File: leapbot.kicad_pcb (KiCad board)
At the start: 2 copper layers, 100 x 100 mm, 97 parts, among them J1 629105150521, J2 Conn_01x04_Male, J3 BM06B-SRSS-TB, J4 BM06B-SRSS-TB, Q1 FDV301N, Q2 FDV301N, SW1 1825910-6, SW2 1825910-6, U1 QRE1113GR, U10 DRV8872DDA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

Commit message: Add silkscreen annotations and logo, update titleblocks
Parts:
- added SYM1: LOGO, leapbot:logo, F.Cu at (84.5, 132.2)
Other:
- board text added: "+"
- board text added: "-"
- board text added: "3S BATTERY"
- board text added: "BATT"
- board text added: "BOOT"
- board text added: "ESP32"
- board text added: "LED0"
- board text added: "LED1"
- board text added: "LED2"
- board text added: "LED3"
- board text added: "LED4"
- board text added: "LED5"
- board text added: "LED6"
- board text added: "LED7"
- board text added: "LeapBot Rev 0.0.0 - 2020 github.com/hoani"
- board text added: "MOTOR LEFT"
- board text added: "MOTOR RIGHT"
- board text added: "RESET"

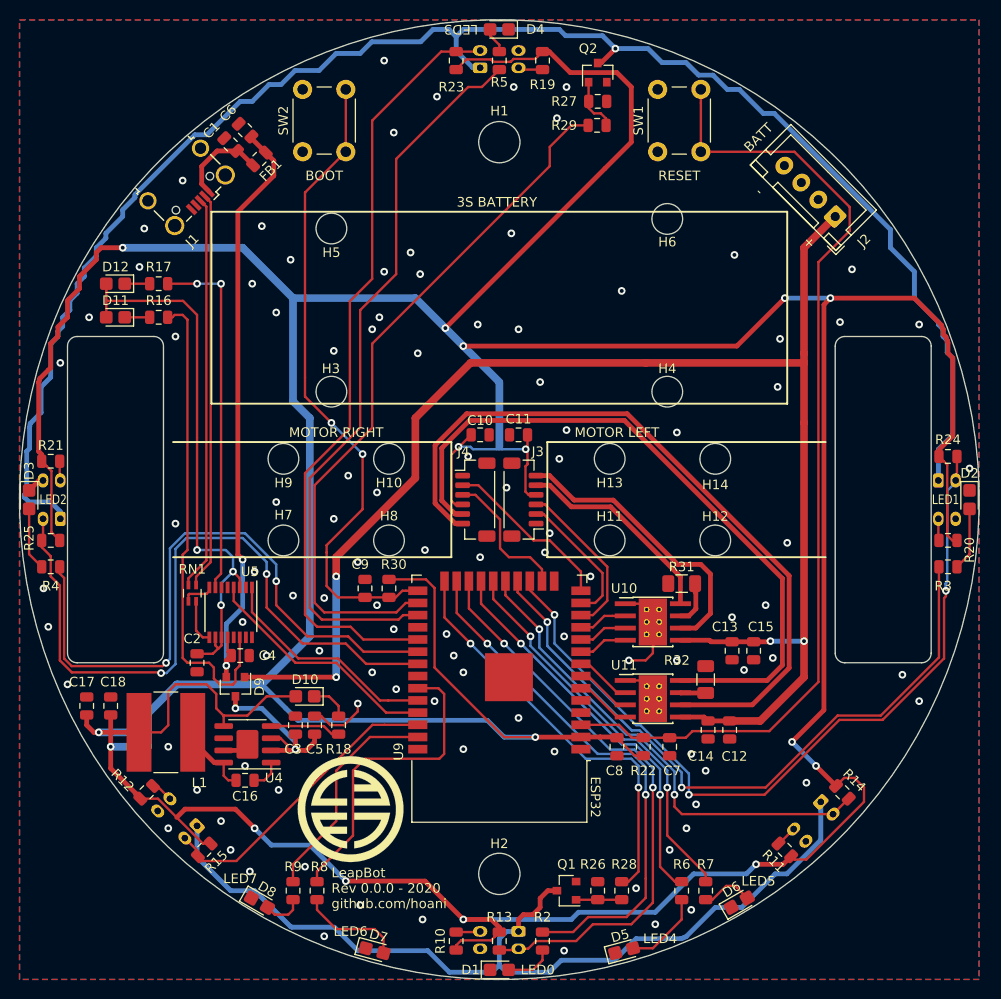
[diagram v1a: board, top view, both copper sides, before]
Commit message: Corrected some ADC assignments
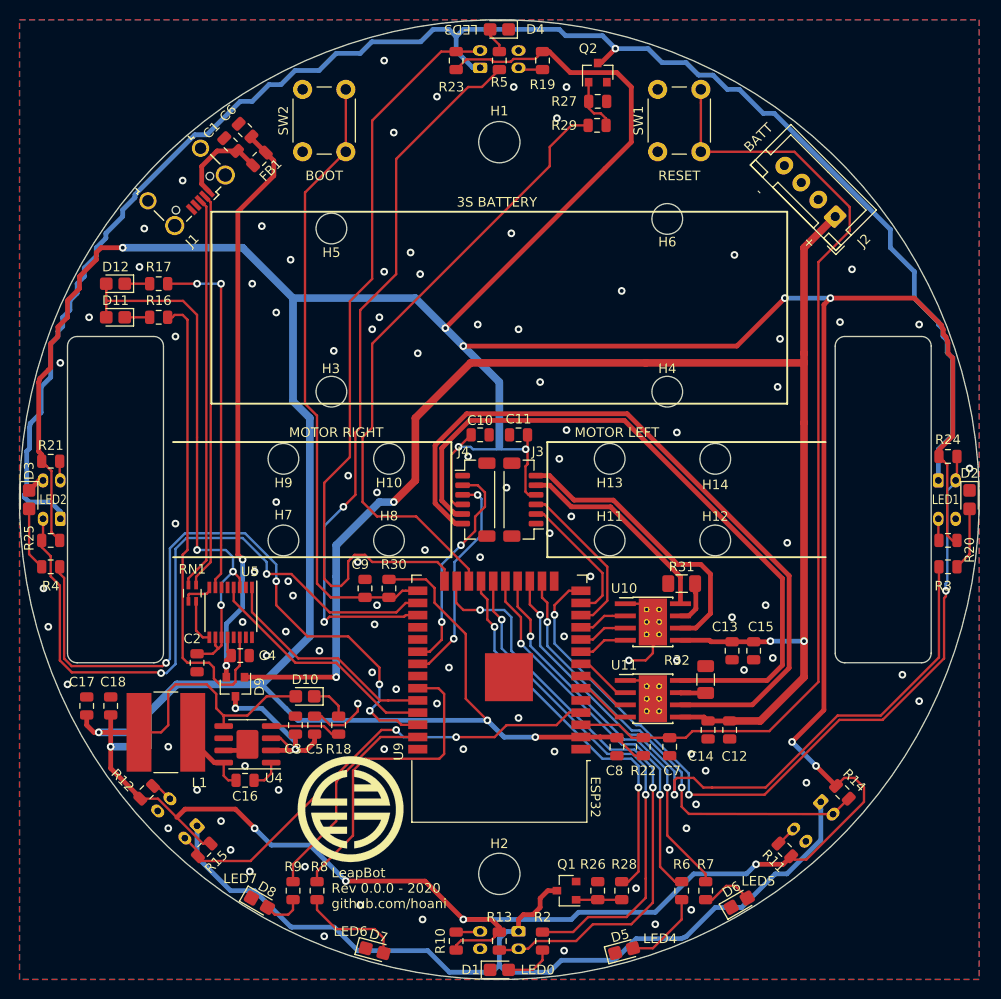
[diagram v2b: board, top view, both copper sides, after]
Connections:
- U9 pad 14: /M2_EB -> /LS_BL
- U9 pad 16: /M2_EA -> /LS_FL
- U9 pad 17: /LS_BL -> /LED1
- U9 pad 18: /LED1 -> /LED5
- U9 pad 19: /LS_FL -> /LED4
- U9 pad 20: /LED5 -> /LED0
- U9 pad 21: /LED4 -> /LS_PF
- U9 pad 22: /LS_FF -> /LS_PB
- U9 pad 23: /LED0 -> /LS_FF
- U9 pad 24: /LS_PF -> /LS_BB
- U9 pad 26: /LS_PB -> /LS_BR
- U9 pad 29: /LS_BB -> Net-(U9-Pad29)
- U9 pad 30: /LED2 -> /M2_EB
- U9 pad 31: /LS_BR -> /M2_EA
- U9 pad 36: /LS_FR -> /LED2
- U9 pad 4: Net-(U9-Pad4) -> /LS_FR
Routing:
- net /LS_FR: track 31.5 -> 49.6 mm, vias 0 -> 2
- net /LS_PB: track 74.2 -> 65.2 mm
- net /M2_EA: track 14.5 -> 22.7 mm, vias 0 -> 2
- net /LED2: track 67.0 -> 74.2 mm, vias 2 -> 4
- net +3V3: track 585.2 -> 579.5 mm, vias 16 -> 17
- net /M2_EB: track 18.0 -> 22.9 mm, vias 0 -> 2
- net /LS_BR: track 74.5 -> 70.6 mm
- net /LS_FF: track 61.0 -> 64.0 mm
- net /LED1: track 70.9 -> 73.7 mm
- net /BOOT_OP: track 67.8 -> 65.2 mm, vias 2 -> 0
- net /LS_PF: track 43.6 -> 41.0 mm
- net /LS_FL: track 50.6 -> 48.4 mm
- net /LED0: track 55.5 -> 53.4 mm
- net /LED5: track 41.2 -> 40.2 mm
- net /LED4: track 41.2 -> 40.2 mm
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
